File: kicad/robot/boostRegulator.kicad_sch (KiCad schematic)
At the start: 22 parts, among them U5 LSF0102DCTR, U6 MAX77857

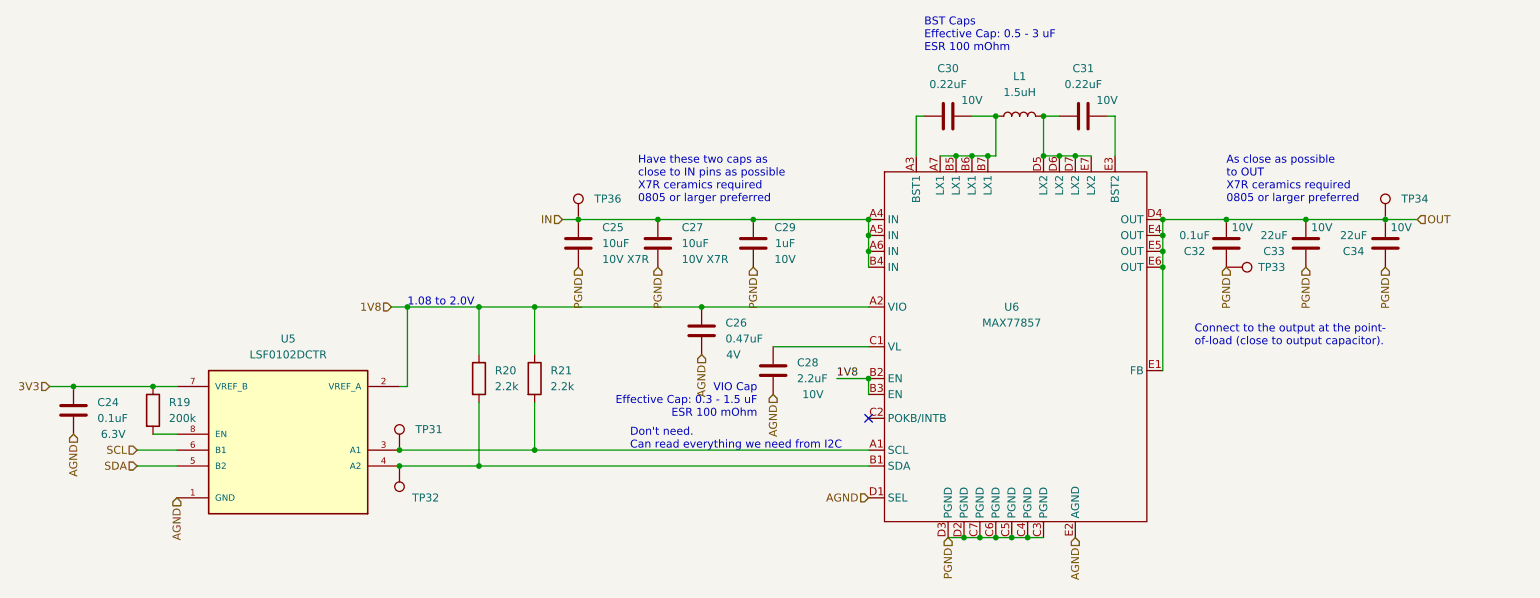
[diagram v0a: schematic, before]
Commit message: Add current breaks between each section of hardware.
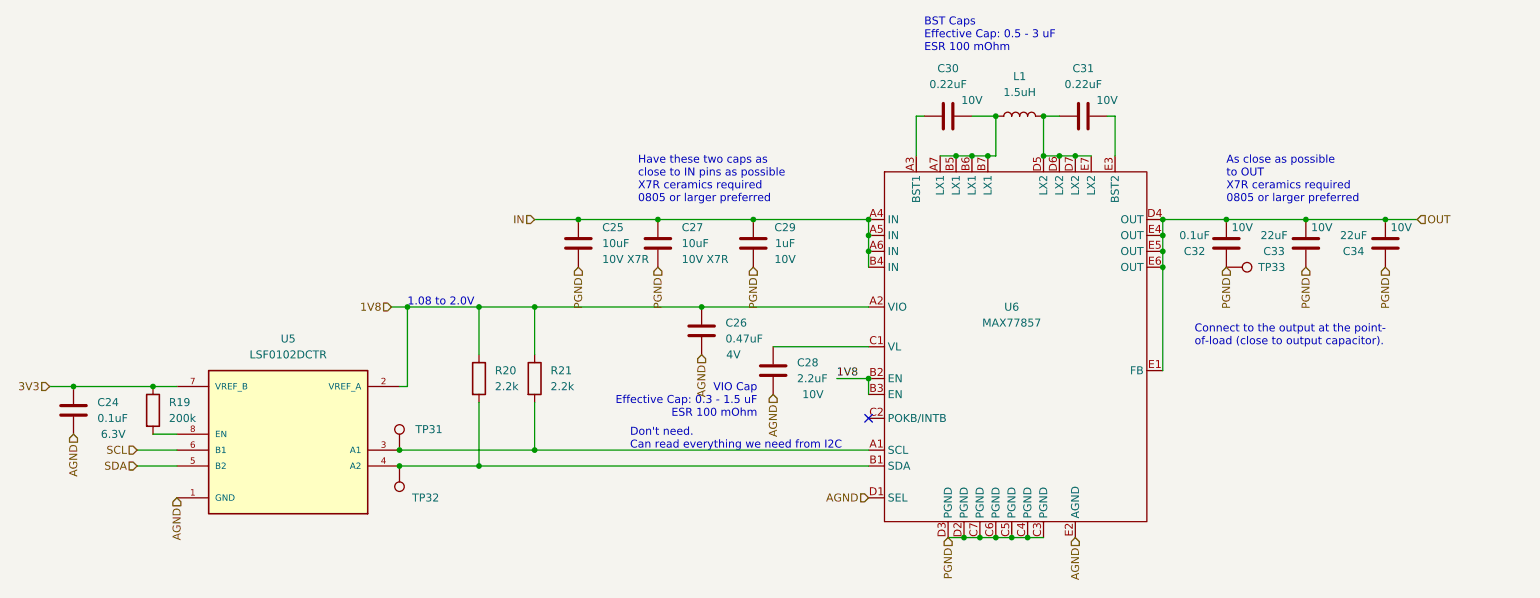
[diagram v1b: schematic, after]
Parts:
- removed TP34, TP36: TP5002, TestPoint:KEYSTONE_5002, symbol Connector:TestPoint
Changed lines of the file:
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@@
     (stroke (width 0) (type default))
   )
-  (wire (pts (xy 122.555 90.17) (xy 125.095 90.17))
+  (wire (pts (xy 118.11 90.17) (xy 125.095 90.17))
     (stroke (width 0) (type default))
   )
@@
     (effects (font (size 1.27 1.27)) (justify right))
   )
-  (hierarchical_label "IN" (shape input) (at 122.555 90.17 180) (fields_autoplaced)
+  (hierarchical_label "IN" (shape input) (at 118.11 90.17 180) (fields_autoplaced)
     (effects (font (size 1.27 1.27)) (justify right))
   )
@@
     )
   )
-  (symbol (lib_id "Connector:TestPoint") (at 125.095 90.17 0) (unit 1)
-    (in_bom yes) (on_board yes) (dnp no) (fields_autoplaced)
-    (property "Reference" "TP36" (at 127.635 86.8679 0)
-      (effects (font (size 1.27 1.27)) (justify left))
-    )
-    (property "Value" "TP5002" (at 127.635 88.1379 0)
-      (effects (font (size 1.27 1.27)) (justify left) hide)
-    )
-    (property "Footprint" "TestPoint:KEYSTONE_5002" (at 130.175 90.17 0)
-      (effects (font (size 1.27 1.27)) hide)
-    )
-    (property "Datasheet" "~" (at 130.175 90.17 0)
-      (effects (font (size 1.27 1.27)) hide)
-    )
-    (property "Manufacturer" "Keystone Electronics" (at 125.095 90.17 0)
-      (effects (font (size 1.27 1.27)) hide)
-    )
-    (property "Part Number" "5002" (at 125.095 90.17 0)
-      (effects (font (size 1.27 1.27)) hide)
-    )
-    (pin "1")
-    (instances
-      (project "robot"
-        (path "/0c7b298e-2d07-4b1f-b033-e95f02d45089/427922e5-a943-4728-8788-709c0c3b2395"
-          (reference "TP36") (unit 1)
-        )
-      )
-    )
-  )
   (symbol (lib_id "Device:C") (at 156.21 114.3 0) (unit 1)
     (in_bom yes) (on_board yes) (dnp no)
@@
         )
       )
-    )
-  )
-  (symbol (lib_id "Connector:TestPoint") (at 254 90.17 0) (unit 1)
-    (in_bom yes) (on_board yes) (dnp no) (fields_autoplaced)
-    (property "Reference" "TP34" (at 256.54 86.8679 0)
-      (effects (font (size 1.27 1.27)) (justify left))
-    )
-    (property "Value" "TP5002" (at 256.54 88.1379 0)
-      (effects (font (size 1.27 1.27)) (justify left) hide)
-    )
-    (property "Footprint" "TestPoint:KEYSTONE_5002" (at 259.08 90.17 0)
-      (effects (font (size 1.27 1.27)) hide)
-    )
-    (property "Datasheet" "~" (at 259.08 90.17 0)
-      (effects (font (size 1.27 1.27)) hide)
-    )
-    (property "Description" "OUT" (at 254 90.17 0)
-      (effects (font (size 1.27 1.27)) hide)
-    )
-    (property "Manufacturer" "Keystone Electronics" (at 254 90.17 0)
-      (effects (font (size 1.27 1.27)) hide)
-    )
-    (property "Part Number" "5002" (at 254 90.17 0)
-      (effects (font (size 1.27 1.27)) hide)
-    )
-    (pin "1")
-    (instances
-      (project "robot"
-        (path "/0c7b298e-2d07-4b1f-b033-e95f02d45089/427922e5-a943-4728-8788-709c0c3b2395"
-          (reference "TP34") (unit 1)
-        )
-      )

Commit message: Hide all test point values keep ref
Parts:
- TP31, TP32, TP33: value TP5002 -> TestPoint
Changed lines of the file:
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@@
       (effects (font (size 1.27 1.27)) (justify right))
     )
-    (property "Value" "TP5002" (at 99.06 131.5721 0)
+    (property "Value" "TestPoint" (at 99.06 131.5721 0)
       (effects (font (size 1.27 1.27)) (justify left) hide)
     )
@@
       (effects (font (size 1.27 1.27)) (justify left))
     )
-    (property "Value" "TP5002" (at 230.6321 100.33 0)
+    (property "Value" "TestPoint" (at 230.6321 100.33 0)
       (effects (font (size 1.27 1.27)) (justify left) hide)
     )
@@
       (effects (font (size 1.27 1.27)) (justify left))
     )
-    (property "Value" "TP5002" (at 99.06 124.9679 0)
+    (property "Value" "TestPoint" (at 99.06 124.9679 0)
       (effects (font (size 1.27 1.27)) (justify left) hide)
     )

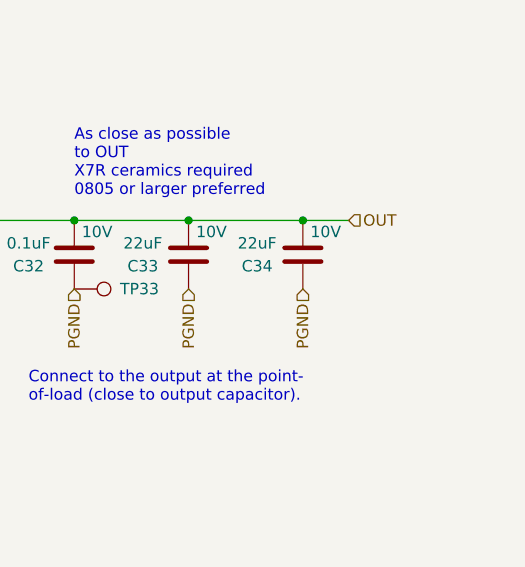
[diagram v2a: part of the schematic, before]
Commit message: Adding DNP bulk capacitance to SYS and Vboost rails. Some populared
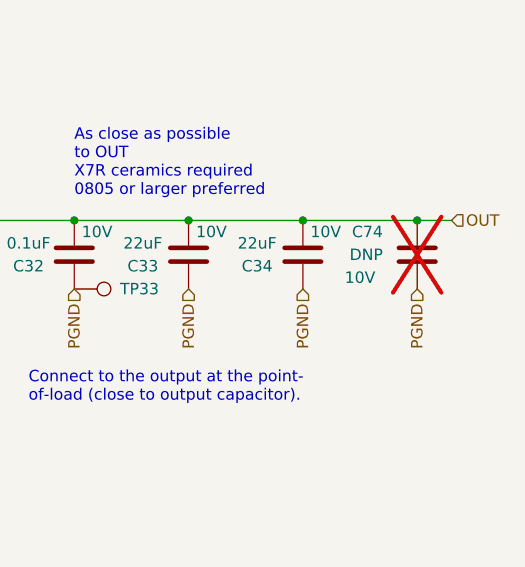
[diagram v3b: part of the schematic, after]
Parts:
- added C74: DNP, Capacitor_SMD:C_0805_2012Metric, symbol Device:C
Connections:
- net OUT: now also C74.1
- net PGND: now also C74.2
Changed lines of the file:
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@@
   (junction (at 191.77 73.66) (diameter 0) (color 0 0 0 0)
+  )
+  (junction (at 266.7 90.17) (diameter 0) (color 0 0 0 0)
   )
   (junction (at 171.45 115.57) (diameter 0) (color 0 0 0 0)
@@
     (stroke (width 0) (type default))
   )
+  (wire (pts (xy 266.7 90.17) (xy 270.51 90.17))
+    (stroke (width 0) (type default))
+  )
   (wire (pts (xy 182.88 80.01) (xy 185.42 80.01))
     (stroke (width 0) (type default))
@@
     (stroke (width 0) (type default))
   )
-  (wire (pts (xy 254 90.17) (xy 259.08 90.17))
+  (wire (pts (xy 254 90.17) (xy 266.7 90.17))
     (stroke (width 0) (type default))
   )
@@
     (effects (font (size 1.27 1.27)) (justify right))
   )
+  (hierarchical_label "PGND" (shape input) (at 266.7 97.79 270) (fields_autoplaced)
+    (effects (font (size 1.27 1.27)) (justify right))
+  )
   (hierarchical_label "PGND" (shape input) (at 125.095 97.79 270) (fields_autoplaced)
     (effects (font (size 1.27 1.27)) (justify right))
@@
     (effects (font (size 1.27 1.27)) (justify right))
   )
-  (hierarchical_label "OUT" (shape input) (at 259.08 90.17 0) (fields_autoplaced)
+  (hierarchical_label "OUT" (shape input) (at 270.51 90.17 0) (fields_autoplaced)
     (effects (font (size 1.27 1.27)) (justify left))
   )
@@
         )
       )
+    )
+  )
+  (symbol (lib_id "Device:C") (at 266.7 93.98 0) (mirror y) (unit 1)
+    (in_bom no) (on_board yes) (dnp yes)
+    (property "Reference" "C74" (at 262.89 91.4399 0)
+      (effects (font (size 1.27 1.27)) (justify left))
+    )
+    (property "Value" "DNP" (at 262.89 93.9799 0)
+      (effects (font (size 1.27 1.27)) (justify left))
+    )
+    (property "Footprint" "Capacitor_SMD:C_0805_2012Metric" (at 265.7348 97.79 0)
+      (effects (font (size 1.27 1.27)) hide)
+    )
+    (property "Datasheet" "~" (at 266.7 93.98 0)
+      (effects (font (size 1.27 1.27)) hide)
+    )
+    (property "Description" "10V" (at 260.35 96.52 0)
+      (effects (font (size 1.27 1.27)))
+    )
+    (property "Manufacturer" "DNP" (at 266.7 93.98 0)
+      (effects (font (size 1.27 1.27)) hide)
+    )
+    (property "Part Number" "DNP" (at 266.7 93.98 0)
+      (effects (font (size 1.27 1.27)) hide)
+    )
+    (pin "1")
+    (pin "2")
+    (instances
+      (project "robot"
+        (path "/0c7b298e-2d07-4b1f-b033-e95f02d45089/3b7e5198-fb12-4059-9002-c176f652e784"
+          (reference "C74") (unit 1)
+        )
+        (path "/0c7b298e-2d07-4b1f-b033-e95f02d45089/4bf796fd-fdb4-45d1-808a-a634d5f4571e"
+          (reference "C89") (unit 1)
+        )
+        (path "/0c7b298e-2d07-4b1f-b033-e95f02d45089/427922e5-a943-4728-8788-709c0c3b2395"
+          (reference "C91") (unit 1)
+        )
+      )

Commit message: updated all footprint fields in schematic symbols with local robot ones
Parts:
- C24, C29, C32: footprint Capacitor_SMD:C_0402_1005Metric -> robot:C_0402_1005Metric
- C25, C26, C27, C28, C30, C31, C33, C34: footprint Capacitor_SMD:C_0603_1608Metric -> robot:C_0603_1608Metric
- C74: footprint Capacitor_SMD:C_0805_2012Metric -> robot:C_0805_2012Metric
- L1: footprint custom_inductors:NRS6028T1R5NMGJ -> robot:NRS6028T1R5NMGJ
- R19, R20, R21: footprint Resistor_SMD:R_0603_1608Metric -> robot:R_0603_1608Metric
- TP31, TP32, TP33: footprint TestPoint:KEYSTONE_5002 -> robot:KEYSTONE_5002
- U5: footprint Snapeda:SOP65P400X130-8N -> robot:SOP65P400X130-8N
- U6: footprint Package_BGA:WLP-35_7x5_2.828x2.028mm -> robot:WLP-35_7x5_2.828x2.028mm
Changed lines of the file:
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@@
       (effects (font (size 1.27 1.27)))
     )
-    (property "Footprint" "Package_BGA:WLP-35_7x5_2.828x2.028mm" (at 194.31 106.68 0)
+    (property "Footprint" "robot:WLP-35_7x5_2.828x2.028mm" (at 194.31 106.68 0)
       (effects (font (size 1.27 1.27)) hide)
     )
@@
       (effects (font (size 1.27 1.27)) (justify left))
     )
-    (property "Footprint" "Capacitor_SMD:C_0603_1608Metric" (at 157.1752 118.11 0)
+    (property "Footprint" "robot:C_0603_1608Metric" (at 157.1752 118.11 0)
       (effects (font (size 1.27 1.27)) hide)
     )
@@
       (effects (font (size 1.27 1.27)))
     )
-    (property "Footprint" "Snapeda:SOP65P400X130-8N" (at 78.74 127 0)
+    (property "Footprint" "robot:SOP65P400X130-8N" (at 78.74 127 0)
       (effects (font (size 1.27 1.27)) (justify left bottom) hide)
     )
@@
       (effects (font (size 1.27 1.27)))
     )
-    (property "Footprint" "Capacitor_SMD:C_0402_1005Metric" (at 227.6348 90.17 0)
+    (property "Footprint" "robot:C_0402_1005Metric" (at 227.6348 90.17 0)
       (effects (font (size 1.27 1.27)) hide)
     )
@@
       (effects (font (size 1.27 1.27)) (justify left))
     )
-    (property "Footprint" "Capacitor_SMD:C_0603_1608Metric" (at 138.7602 97.79 0)
+    (property "Footprint" "robot:C_0603_1608Metric" (at 138.7602 97.79 0)
       (effects (font (size 1.27 1.27)) hide)
     )
@@
       (effects (font (size 1.27 1.27)) (justify left))
     )
-    (property "Footprint" "Resistor_SMD:R_0603_1608Metric" (at 107.442 115.57 90)
+    (property "Footprint" "robot:R_0603_1608Metric" (at 107.442 115.57 90)
       (effects (font (size 1.27 1.27)) hide)
     )
@@
       (effects (font (size 1.27 1.27)) (justify left))
     )
-    (property "Footprint" "Capacitor_SMD:C_0603_1608Metric" (at 126.0602 97.79 0)
+    (property "Footprint" "robot:C_0603_1608Metric" (at 126.0602 97.79 0)
       (effects (font (size 1.27 1.27)) hide)
     )
@@
       (effects (font (size 1.27 1.27)) (justify left))
     )
-    (property "Footprint" "Capacitor_SMD:C_0402_1005Metric" (at 45.4152 124.46 0)
+    (property "Footprint" "robot:C_0402_1005Metric" (at 45.4152 124.46 0)
       (effects (font (size 1.27 1.27)) hide)
     )
@@
       (effects (font (size 1.27 1.27)) (justify left) hide)
     )
-    (property "Footprint" "TestPoint:KEYSTONE_5002" (at 101.6 129.54 0)
+    (property "Footprint" "robot:KEYSTONE_5002" (at 101.6 129.54 0)
       (effects (font (size 1.27 1.27)) hide)
     )
@@
       (effects (font (size 1.27 1.27)) (justify left) hide)
     )
-    (property "Footprint" "TestPoint:KEYSTONE_5002" (at 228.6 102.87 0)
+    (property "Footprint" "robot:KEYSTONE_5002" (at 228.6 102.87 0)
       (effects (font (size 1.27 1.27)) hide)
     )
@@
       (effects (font (size 1.27 1.27)))
     )
-    (property "Footprint" "Capacitor_SMD:C_0402_1005Metric" (at 152.0698 90.17 0)
+    (property "Footprint" "robot:C_0402_1005Metric" (at 152.0698 90.17 0)
       (effects (font (size 1.27 1.27)) hide)
     )
@@
       (effects (font (size 1.27 1.27)))
     )
-    (property "Footprint" "Capacitor_SMD:C_0603_1608Metric" (at 253.0348 90.17 0)
+    (property "Footprint" "robot:C_0603_1608Metric" (at 253.0348 90.17 0)
       (effects (font (size 1.27 1.27)) hide)
     )
@@
       (effects (font (size 1.27 1.27)))
     )
-    (property "Footprint" "custom_inductors:NRS6028T1R5NMGJ" (at 195.58 73.66 0)
+    (property "Footprint" "robot:NRS6028T1R5NMGJ" (at 195.58 73.66 0)
       (effects (font (size 1.27 1.27)) hide)
     )
@@
       (effects (font (size 1.27 1.27)) (justify left) hide)
     )
-    (property "Footprint" "TestPoint:KEYSTONE_5002" (at 101.6 127 0)
+    (property "Footprint" "robot:KEYSTONE_5002" (at 101.6 127 0)
       (effects (font (size 1.27 1.27)) hide)
     )
@@
       (effects (font (size 1.27 1.27)))
     )
-    (property "Footprint" "Capacitor_SMD:C_0603_1608Metric" (at 240.3348 90.17 0)
+    (property "Footprint" "robot:C_0603_1608Metric" (at 240.3348 90.17 0)
       (effects (font (size 1.27 1.27)) hide)
     )
@@
       (effects (font (size 1.27 1.27)))
     )
-    (property "Footprint" "Capacitor_SMD:C_0603_1608Metric" (at 187.96 72.6948 0)
+    (property "Footprint" "robot:C_0603_1608Metric" (at 187.96 72.6948 0)
       (effects (font (size 1.27 1.27)) hide)
     )
@@
       (effects (font (size 1.27 1.27)) (justify left))
     )
-    (property "Footprint" "Resistor_SMD:R_0603_1608Metric" (at 55.372 120.65 90)
+    (property "Footprint" "robot:R_0603_1608Metric" (at 55.372 120.65 90)
       (effects (font (size 1.27 1.27)) hide)
     )
@@
       (effects (font (size 1.27 1.27)) (justify left))
     )
-    (property "Footprint" "Capacitor_SMD:C_0603_1608Metric" (at 145.7452 111.76 0)
+    (property "Footprint" "robot:C_0603_1608Metric" (at 145.7452 111.76 0)
       (effects (font (size 1.27 1.27)) hide)
     )
@@
       (effects (font (size 1.27 1.27)))
     )
-    (property "Footprint" "Capacitor_SMD:C_0603_1608Metric" (at 209.55 72.6948 0)
+    (property "Footprint" "robot:C_0603_1608Metric" (at 209.55 72.6948 0)
       (effects (font (size 1.27 1.27)) hide)
     )
@@
       (effects (font (size 1.27 1.27)) (justify left))
     )
-    (property "Footprint" "Resistor_SMD:R_0603_1608Metric" (at 116.332 115.57 90)
+    (property "Footprint" "robot:R_0603_1608Metric" (at 116.332 115.57 90)
       (effects (font (size 1.27 1.27)) hide)
     )
@@
       (effects (font (size 1.27 1.27)) (justify left))
     )
-    (property "Footprint" "Capacitor_SMD:C_0805_2012Metric" (at 265.7348 97.79 0)
-      (effects (font (size 1.27 1.27)) hide)
-    )
+    (property "Footprint" "robot:C_0805_2012Metric" (at 265.7348 97.79 0)
+      (effects (font (size 1.27 1.27)) hide)
+    )
